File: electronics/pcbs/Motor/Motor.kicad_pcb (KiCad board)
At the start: 2 copper layers, 68.6 x 53.3 mm, 8 parts, among them P1 Power, P2 Analog, P3 Digital, P4 Digital, P5 CONN_01X01, P6 CONN_01X01, P7 CONN_01X01, P8 CONN_01X01

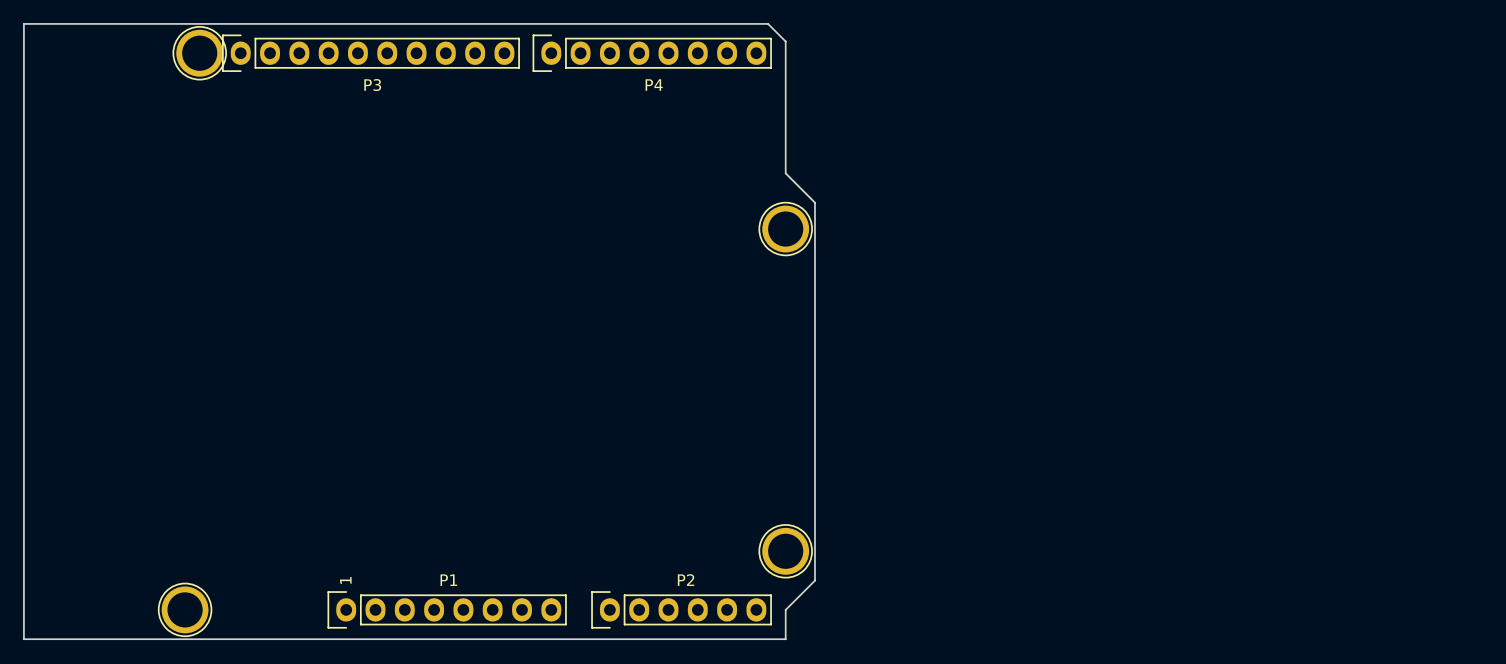
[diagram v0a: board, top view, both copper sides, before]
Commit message: Motor PCB: First draft of PCB.
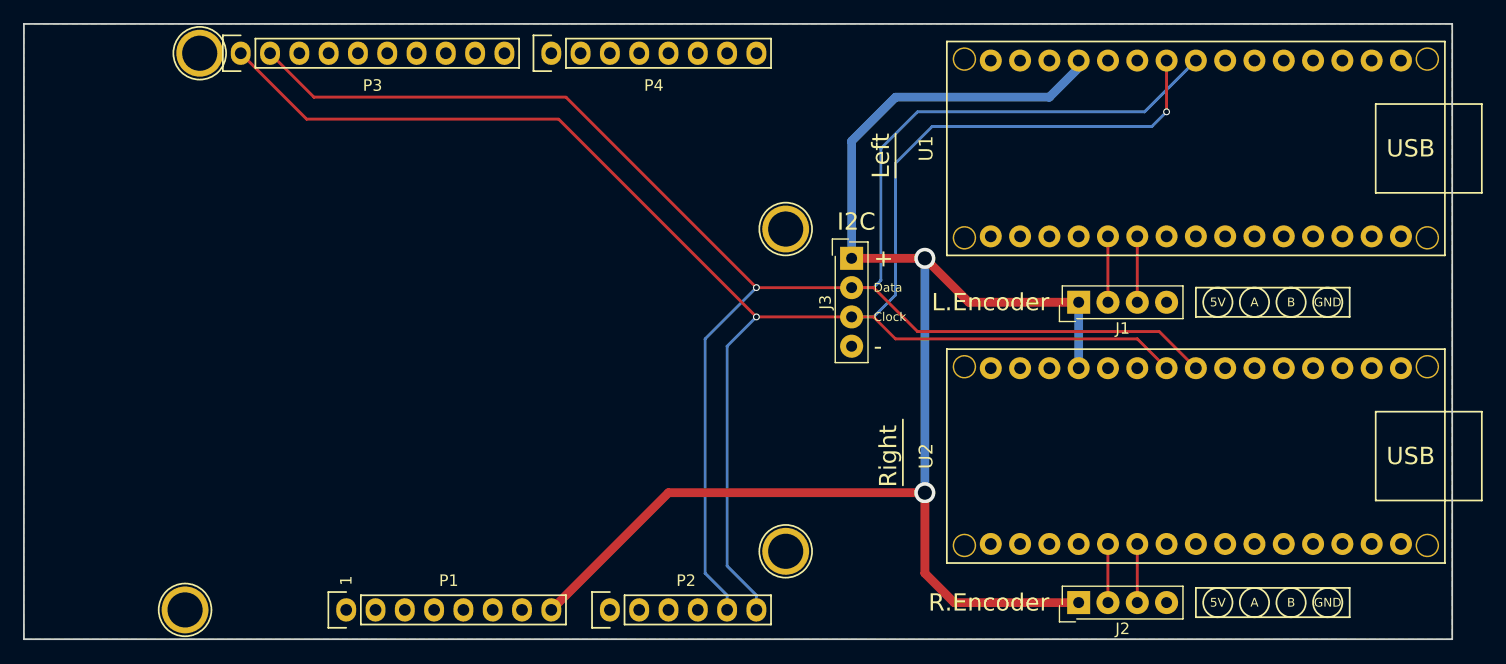
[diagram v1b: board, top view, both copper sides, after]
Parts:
- added J1: Left Encoder, Connectors_Samtec:SL-104-X-XX_1x04, F.Cu at (202.4, 97.2)
- added J2: Right Encoder, Connectors_Samtec:SL-104-X-XX_1x04, F.Cu at (202.4, 123.2)
- added J3: I2C Bus, Connectors_Samtec:SL-104-X-XX_1x04, F.Cu at (182.8, 93.3)
- added U1: Left Nano, Arduino_Nano:Arduino_Nano, F.Cu at (234.2, 76.2)
- added U2: Right Nano, Arduino_Nano:Arduino_Nano, F.Cu at (234.2, 102.9)
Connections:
- net +3V3 renamed Net-(P1-Pad4)
- P1 pad 5: +5V -> Net-(P1-Pad5)
- P1 pad 8: /Vin -> +5V
- P5 pad 1: Net-(P5-Pad1) -> GND
- P6 pad 1: Net-(P6-Pad1) -> GND
- P7 pad 1: Net-(P7-Pad1) -> GND
- P8 pad 1: Net-(P8-Pad1) -> GND
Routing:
- net /A4(SDA): track 0.00 -> 166.8 mm, vias 0 -> 1
- net /A5(SCL): track 0.00 -> 164.9 mm, vias 0 -> 2
- net +5V: track 0.00 -> 138.4 mm, vias 0 -> 2
- net /L_ENC_B: track 0.00 -> 5.72 mm
- net /L_ENC_A: track 0.00 -> 5.72 mm
- net /R_ENC_B: track 0.00 -> 5.08 mm
- net /R_ENC_A: track 0.00 -> 5.08 mm
- added copper zone on B.Cu, net GND
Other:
- board size 68.6 x 53.3 mm -> 123.8 x 53.3 mm
- net class Ground added: clearance 0.2, trace_width 0.762, via_dia 1.8288, via_drill 1.2192
- net class Power added: clearance 0.2, trace_width 0.762, via_dia 1.8288, via_drill 1.2192
- board text added: "+"
- board text added: "-"
- board text added: "5V"
- board text added: "A"
- board text added: "B"
- board text added: "Clock"
- board text added: "Data"
- board text added: "GND"
- board text added: "I2C"
- board text added: "L.Encoder"
- board text added: "Left"
- board text added: "R.Encoder"
- board text added: "Right"
- board text added: "USB"
